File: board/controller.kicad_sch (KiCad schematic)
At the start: 26 parts, among them U3 W5500, Y2 25MHz

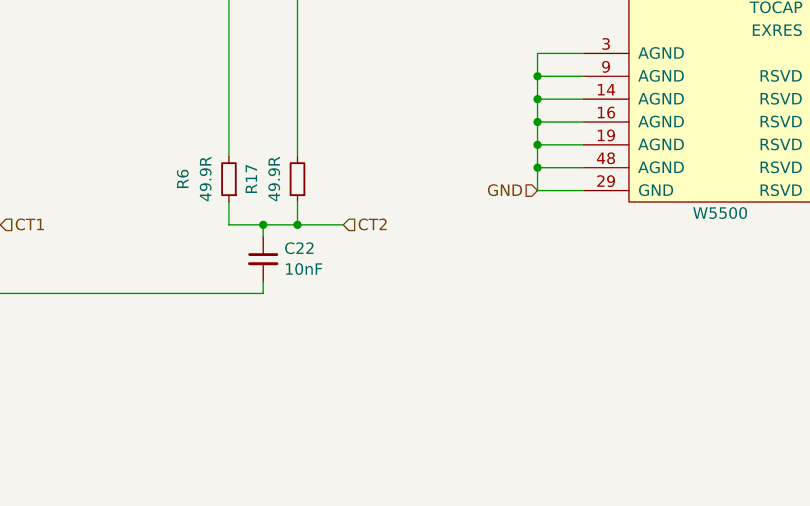
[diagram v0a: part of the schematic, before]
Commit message: updated to use v1.1 of b078 to work with shorted center tap magjacks
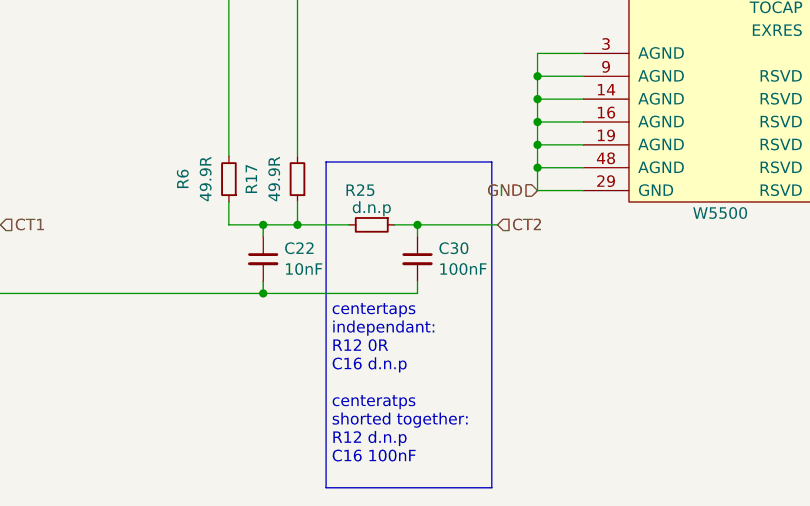
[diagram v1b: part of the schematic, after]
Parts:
- added C30: 100nF, Capacitor_SMD:C_0603_1608Metric, symbol Device:C_Small
- added R25: d.n.p, Resistor_SMD:R_0805_2012Metric, symbol Device:R_Small
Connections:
- net CT2: now also C30.1, R25.1; no longer C22.1, R17.1, R6.1
- net GND: now also C30.2
- new net: C22.1, R17.1, R25.2, R6.1
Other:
- note added: "centertaps independant: R12 0R C16 d.n.p centeratps shorted together: R12 d.n.p C16 100nF"
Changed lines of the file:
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@@
   (junction (at 176.53 92.71) (diameter 0) (color 0 0 0 0)
   )
+  (junction (at 96.52 87.63) (diameter 0) (color 0 0 0 0)
+  )
+  (junction (at 80.01 50.8) (diameter 0) (color 0 0 0 0)
+  )
+  (junction (at 105.41 49.53) (diameter 0) (color 0 0 0 0)
+  )
+  (junction (at 95.25 64.77) (diameter 0) (color 0 0 0 0)
+  )
+  (junction (at 179.07 116.84) (diameter 0) (color 0 0 0 0)
+  )
+  (junction (at 163.83 92.71) (diameter 0) (color 0 0 0 0)
+  )
+  (junction (at 176.53 82.55) (diameter 0) (color 0 0 0 0)
+  )
+  (junction (at 105.41 59.69) (diameter 0) (color 0 0 0 0)
+  )
+  (junction (at 72.39 64.77) (diameter 0) (color 0 0 0 0)
+  )
+  (junction (at 162.56 44.45) (diameter 0) (color 0 0 0 0)
+  )
+  (junction (at 162.56 113.03) (diameter 0) (color 0 0 0 0)
+  )
+  (junction (at 123.19 110.49) (diameter 0) (color 0 0 0 0)
+  )
+  (junction (at 163.83 82.55) (diameter 0) (color 0 0 0 0)
+  )
+  (junction (at 162.56 107.95) (diameter 0) (color 0 0 0 0)
+  )
+  (junction (at 87.63 50.8) (diameter 0) (color 0 0 0 0)
+  )
+  (junction (at 87.63 64.77) (diameter 0) (color 0 0 0 0)
+  )
+  (junction (at 62.23 92.71) (diameter 0) (color 0 0 0 0)
+  )
+  (junction (at 189.23 116.84) (diameter 0) (color 0 0 0 0)
+  )
+  (junction (at 105.41 54.61) (diameter 0) (color 0 0 0 0)
+  )
+  (junction (at 72.39 50.8) (diameter 0) (color 0 0 0 0)
+  )
+  (junction (at 88.9 90.17) (diameter 0) (color 0 0 0 0)
+  )
+  (junction (at 123.19 115.57) (diameter 0) (color 0 0 0 0)
+  )
+  (junction (at 162.56 116.84) (diameter 0) (color 0 0 0 0)
+  )
+  (junction (at 92.71 129.54) (diameter 0) (color 0 0 0 0)
+  )
+  (junction (at 109.855 121.92) (diameter 0) (color 0 0 0 0)
+  )
   (junction (at 96.52 121.92) (diameter 0) (color 0 0 0 0)
-  )
-  (junction (at 96.52 87.63) (diameter 0) (color 0 0 0 0)
-  )
-  (junction (at 80.01 50.8) (diameter 0) (color 0 0 0 0)
-  )
-  (junction (at 105.41 49.53) (diameter 0) (color 0 0 0 0)
-  )
-  (junction (at 95.25 64.77) (diameter 0) (color 0 0 0 0)
-  )
-  (junction (at 179.07 116.84) (diameter 0) (color 0 0 0 0)
-  )
-  (junction (at 163.83 92.71) (diameter 0) (color 0 0 0 0)
-  )
-  (junction (at 176.53 82.55) (diameter 0) (color 0 0 0 0)
-  )
-  (junction (at 105.41 59.69) (diameter 0) (color 0 0 0 0)
-  )
-  (junction (at 72.39 64.77) (diameter 0) (color 0 0 0 0)
-  )
-  (junction (at 162.56 44.45) (diameter 0) (color 0 0 0 0)
-  )
-  (junction (at 162.56 113.03) (diameter 0) (color 0 0 0 0)
-  )
-  (junction (at 123.19 110.49) (diameter 0) (color 0 0 0 0)
-  )
-  (junction (at 163.83 82.55) (diameter 0) (color 0 0 0 0)
-  )
-  (junction (at 162.56 107.95) (diameter 0) (color 0 0 0 0)
-  )
-  (junction (at 87.63 50.8) (diameter 0) (color 0 0 0 0)
-  )
-  (junction (at 87.63 64.77) (diameter 0) (color 0 0 0 0)
-  )
-  (junction (at 62.23 92.71) (diameter 0) (color 0 0 0 0)
-  )
-  (junction (at 189.23 116.84) (diameter 0) (color 0 0 0 0)
-  )
-  (junction (at 105.41 54.61) (diameter 0) (color 0 0 0 0)
-  )
-  (junction (at 72.39 50.8) (diameter 0) (color 0 0 0 0)
-  )
-  (junction (at 88.9 90.17) (diameter 0) (color 0 0 0 0)
-  )
-  (junction (at 123.19 115.57) (diameter 0) (color 0 0 0 0)
-  )
-  (junction (at 162.56 116.84) (diameter 0) (color 0 0 0 0)
   )
   (junction (at 69.85 95.25) (diameter 0) (color 0 0 0 0)
@@
     (stroke (width 0) (type default) (color 0 0 0 0))
   )
-  (wire (pts (xy 96.52 121.92) (xy 101.6 121.92))
-    (stroke (width 0) (type default) (color 0 0 0 0))
-  )
   (wire (pts (xy 88.9 90.17) (xy 102.87 90.17))
     (stroke (width 0) (type default) (color 0 0 0 0))
@@
     (stroke (width 0) (type default) (color 0 0 0 0))
   )
+  (polyline (pts (xy 99.695 151.13) (xy 118.11 151.13))
+    (stroke (width 0) (type default) (color 0 0 0 0))
+  )
   (wire (pts (xy 128.27 49.53) (xy 105.41 49.53))
     (stroke (width 0) (type default) (color 0 0 0 0))
@@
     (stroke (width 0) (type default) (color 0 0 0 0))
   )
+  (polyline (pts (xy 118.11 114.935) (xy 99.695 114.935))
+    (stroke (width 0) (type default) (color 0 0 0 0))
+  )
   (wire (pts (xy 105.41 54.61) (xy 105.41 52.07))
     (stroke (width 0) (type default) (color 0 0 0 0))
@@
     (stroke (width 0) (type default) (color 0 0 0 0))
   )
+  (wire (pts (xy 118.745 121.92) (xy 109.855 121.92))
+    (stroke (width 0) (type default) (color 0 0 0 0))
+  )
   (wire (pts (xy 123.19 110.49) (xy 123.19 113.03))
     (stroke (width 0) (type default) (color 0 0 0 0))
@@
     (stroke (width 0) (type default) (color 0 0 0 0))
   )
+  (wire (pts (xy 109.855 121.92) (xy 109.855 123.19))
+    (stroke (width 0) (type default) (color 0 0 0 0))
+  )
   (wire (pts (xy 83.82 90.17) (xy 88.9 90.17))
     (stroke (width 0) (type default) (color 0 0 0 0))
@@
     (stroke (width 0) (type default) (color 0 0 0 0))
   )
+  (wire (pts (xy 107.315 121.92) (xy 109.855 121.92))
+    (stroke (width 0) (type default) (color 0 0 0 0))
+  )
+  (polyline (pts (xy 99.695 114.935) (xy 99.695 151.13))
+    (stroke (width 0) (type default) (color 0 0 0 0))
+  )
   (wire (pts (xy 95.25 50.8) (xy 105.41 50.8))
     (stroke (width 0) (type default) (color 0 0 0 0))
@@
     (stroke (width 0) (type default) (color 0 0 0 0))
   )
+  (wire (pts (xy 92.71 129.54) (xy 109.855 129.54))
+    (stroke (width 0) (type default) (color 0 0 0 0))
+  )
   (wire (pts (xy 162.56 38.1) (xy 162.56 44.45))
     (stroke (width 0) (type default) (color 0 0 0 0))
@@
     (stroke (width 0) (type default) (color 0 0 0 0))
   )
+  (wire (pts (xy 96.52 121.92) (xy 102.235 121.92))
+    (stroke (width 0) (type default) (color 0 0 0 0))
+  )
   (wire (pts (xy 96.52 121.92) (xy 96.52 119.38))
     (stroke (width 0) (type default) (color 0 0 0 0))
   )
+  (wire (pts (xy 109.855 129.54) (xy 109.855 128.27))
+    (stroke (width 0) (type default) (color 0 0 0 0))
+  )
   (wire (pts (xy 69.85 95.25) (xy 114.3 95.25))
     (stroke (width 0) (type default) (color 0 0 0 0))
@@
   (wire (pts (xy 128.27 52.07) (xy 105.41 52.07))
     (stroke (width 0) (type default) (color 0 0 0 0))
+  )
+  (polyline (pts (xy 118.11 114.935) (xy 118.11 151.13))
+    (stroke (width 0) (type default) (color 0 0 0 0))
+  )
+  (text "centertaps \nindependant:\nR12 0R\nC16 d.n.p\n\ncenteratps\nshorted together:\nR12 d.n.p\nC16 100nF"
+    (at 100.33 148.59 0)
+    (effects (font (size 1.27 1.27)) (justify left bottom))
   )
   (label "XCAP" (at 160.02 97.79 0)
@@
     (effects (font (size 1.27 1.27)) (justify right))
   )
-  (hierarchical_label "CT2" (shape input) (at 101.6 121.92 0)
-    (effects (font (size 1.27 1.27)) (justify left))
-  )
   (hierarchical_label "GND" (shape input) (at 123.19 118.11 180)
     (effects (font (size 1.27 1.27)) (justify right))
@@
   )
   (hierarchical_label "INT" (shape input) (at 190.5 64.77 0)
+    (effects (font (size 1.27 1.27)) (justify left))
+  )
+  (hierarchical_label "CT2" (shape input) (at 118.745 121.92 0)
     (effects (font (size 1.27 1.27)) (justify left))
   )
@@
     )
     (property "Datasheet" "~" (id 3) (at 116.84 95.25 0)
+      (effects (font (size 1.27 1.27)) hide)
+    )
+    (pin "1")
+    (pin "2")
+  )
+  (symbol (lib_id "Device:R_Small") (at 104.775 121.92 270) (unit 1)
+    (in_bom yes) (on_board yes)
+    (property "Reference" "R25" (id 0) (at 103.505 118.11 90))
+    (property "Value" "d.n.p" (id 1) (at 104.775 120.015 90))
+    (property "Footprint" "Resistor_SMD:R_0805_2012Metric" (id 2) (at 104.775 121.92 0)
+      (effects (font (size 1.27 1.27)) hide)
+    )
+    (property "Datasheet" "~" (id 3) (at 104.775 121.92 0)
       (effects (font (size 1.27 1.27)) hide)
     )
@@
     (pin "9")
   )
+  (symbol (lib_id "Device:C_Small") (at 109.855 125.73 0) (unit 1)
+    (in_bom yes) (on_board yes)
+    (property "Reference" "C30" (id 0) (at 112.1918 124.5616 0)
+      (effects (font (size 1.27 1.27)) (justify left))
+    )
+    (property "Value" "100nF" (id 1) (at 112.1918 126.873 0)
+      (effects (font (size 1.27 1.27)) (justify left))
+    )
+    (property "Footprint" "Capacitor_SMD:C_0603_1608Metric" (id 2) (at 109.855 125.73 0)
+      (effects (font (size 1.27 1.27)) hide)
+    )
+    (property "Datasheet" "~" (id 3) (at 109.855 125.73 0)
+      (effects (font (size 1.27 1.27)) hide)
+    )
+    (property "Voltage" "6.3V" (id 4) (at 109.855 125.73 0)
+      (effects (font (size 1.27 1.27)) hide)
+    )
+    (pin "1")
+    (pin "2")
+  )
   (symbol (lib_id "Device:R_Small") (at 110.49 87.63 90) (unit 1)

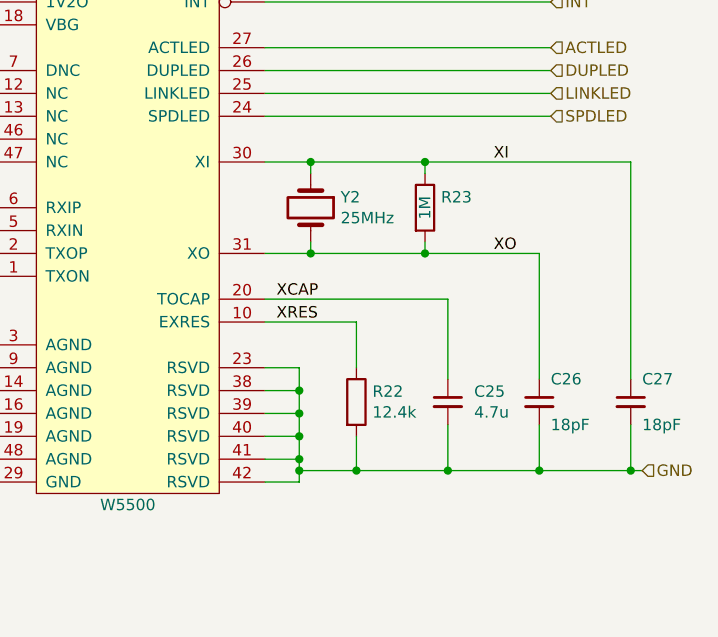
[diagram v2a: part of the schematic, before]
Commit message: moved all components to top layer
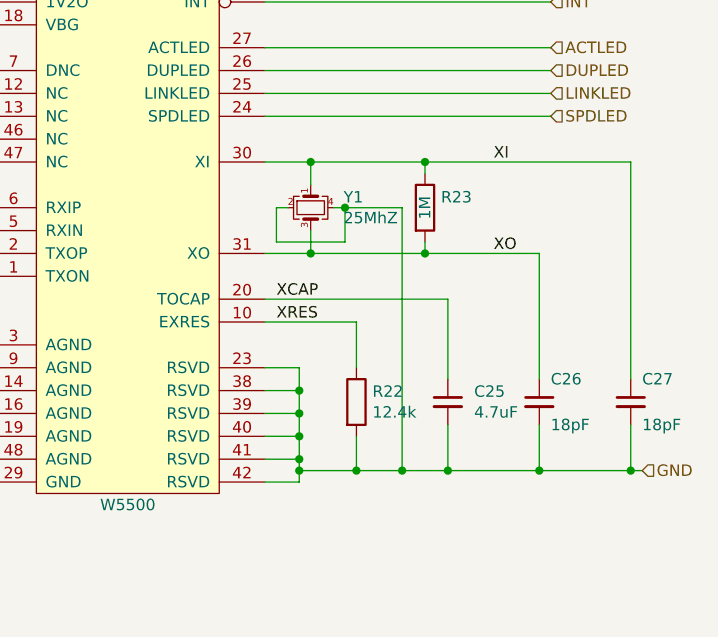
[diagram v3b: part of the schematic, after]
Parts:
- removed Y2: 25MHz, Crystal:Crystal_SMD_5032-2Pin_5.0x3.2mm, symbol Device:Crystal
- added Y1: 25MhZ, Crystal:Crystal_SMD_Abracon_ABM8G-4Pin_3.2x2.5mm, symbol Device:Crystal_GND24_Small
- C16, C17, C19, C21, C22, C23, C26, C27, C30: footprint Capacitor_SMD:C_0603_1608Metric -> Capacitor_SMD:C_0402_1005Metric
- C24: footprint Capacitor_SMD:C_0603_1608Metric -> Capacitor_SMD:C_0402_1005Metric; DigiKey Part Number 1276-1921-1-ND -> (none)
- C25: value 4.7u -> 4.7uF; footprint Capacitor_SMD:C_0603_1608Metric -> Capacitor_SMD:C_0402_1005Metric; DigiKey Part Number 1276-1907-1-ND -> (none)
- R23: footprint Resistor_SMD:R_0603_1608Metric -> Resistor_SMD:R_0402_1005Metric
- R3: footprint Resistor_SMD:R_0805_2012Metric -> Resistor_SMD:R_0603_1608Metric
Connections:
- net GND: now also Y1.2, Y1.4
- net XI: now also Y1.1
- net XO: now also Y1.3
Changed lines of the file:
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@@
   (junction (at 105.41 49.53) (diameter 0) (color 0 0 0 0)
   )
+  (junction (at 167.64 87.63) (diameter 0) (color 0 0 0 0)
+  )
   (junction (at 95.25 64.77) (diameter 0) (color 0 0 0 0)
   )
@@
   )
   (junction (at 162.56 110.49) (diameter 0) (color 0 0 0 0)
+  )
+  (junction (at 173.99 116.84) (diameter 0) (color 0 0 0 0)
   )
   (junction (at 95.25 50.8) (diameter 0) (color 0 0 0 0)
@@
     (stroke (width 0) (type default))
   )
-  (wire (pts (xy 163.83 92.71) (xy 163.83 91.44))
+  (wire (pts (xy 163.83 90.17) (xy 163.83 92.71))
     (stroke (width 0) (type default))
   )
@@
     (stroke (width 0) (type default))
   )
-  (wire (pts (xy 168.91 116.84) (xy 179.07 116.84))
+  (wire (pts (xy 168.91 116.84) (xy 173.99 116.84))
     (stroke (width 0) (type default))
   )
@@
     (stroke (width 0) (type default))
   )
+  (wire (pts (xy 173.99 116.84) (xy 179.07 116.84))
+    (stroke (width 0) (type default))
+  )
   (wire (pts (xy 87.63 64.77) (xy 80.01 64.77))
     (stroke (width 0) (type default))
@@
     (stroke (width 0) (type default))
   )
+  (wire (pts (xy 167.64 87.63) (xy 166.37 87.63))
+    (stroke (width 0) (type default))
+  )
   (wire (pts (xy 72.39 64.77) (xy 64.77 64.77))
     (stroke (width 0) (type default))
@@
     (stroke (width 0) (type default))
   )
+  (wire (pts (xy 173.99 116.84) (xy 173.99 87.63))
+    (stroke (width 0) (type default))
+  )
   (polyline (pts (xy 99.695 114.935) (xy 99.695 151.13))
     (stroke (width 0) (type default))
@@
     (stroke (width 0) (type default))
   )
+  (wire (pts (xy 173.99 87.63) (xy 167.64 87.63))
+    (stroke (width 0) (type default))
+  )
   (wire (pts (xy 162.56 116.84) (xy 162.56 115.57))
     (stroke (width 0) (type default))
@@
     (stroke (width 0) (type default))
   )
+  (wire (pts (xy 167.64 87.63) (xy 167.64 91.44))
+    (stroke (width 0) (type default))
+  )
   (wire (pts (xy 55.88 129.54) (xy 92.71 129.54))
     (stroke (width 0) (type default))
@@
     (stroke (width 0) (type default))
   )
+  (wire (pts (xy 167.64 91.44) (xy 160.02 91.44))
+    (stroke (width 0) (type default))
+  )
   (wire (pts (xy 58.42 92.71) (xy 62.23 92.71))
     (stroke (width 0) (type default))
@@
     (stroke (width 0) (type default))
   )
+  (wire (pts (xy 160.02 91.44) (xy 160.02 87.63))
+    (stroke (width 0) (type default))
+  )
   (wire (pts (xy 96.52 121.92) (xy 96.52 119.38))
     (stroke (width 0) (type default))
@@
     (stroke (width 0) (type default))
   )
+  (wire (pts (xy 160.02 87.63) (xy 161.29 87.63))
+    (stroke (width 0) (type default))
+  )
   (wire (pts (xy 87.63 60.96) (xy 87.63 64.77))
     (stroke (width 0) (type default))
@@
     (stroke (width 0) (type default))
   )
-  (wire (pts (xy 163.83 82.55) (xy 163.83 83.82))
+  (wire (pts (xy 163.83 82.55) (xy 163.83 85.09))
     (stroke (width 0) (type default))
   )
@@
       (effects (font (size 1.27 1.27)) (justify left))
     )
-    (property "Footprint" "Capacitor_SMD:C_0603_1608Metric" (at 95.25 58.42 0)
+    (property "Footprint" "Capacitor_SMD:C_0402_1005Metric" (at 95.25 58.42 0)
       (effects (font (size 1.27 1.27)) hide)
     )
@@
       (effects (font (size 1.27 1.27)) (justify left))
     )
-    (property "Value" "4.7u" (at 181.991 110.363 0)
-      (effects (font (size 1.27 1.27)) (justify left))
-    )
-    (property "Footprint" "Capacitor_SMD:C_0603_1608Metric" (at 179.07 109.22 0)
+    (property "Value" "4.7uF" (at 181.991 110.363 0)
+      (effects (font (size 1.27 1.27)) (justify left))
+    )
+    (property "Footprint" "Capacitor_SMD:C_0402_1005Metric" (at 179.07 109.22 0)
       (effects (font (size 1.27 1.27)) hide)
     )
@@
       (effects (font (size 1.27 1.27)) hide)
     )
-    (property "DigiKey Part Number" "1276-1907-1-ND" (at 179.07 109.22 0)
-      (effects (font (size 1.27 1.27)) hide)
-    )
     (pin "1")
     (pin "2")
@@
       (effects (font (size 1.27 1.27)) (justify left))
     )
-    (property "Footprint" "Capacitor_SMD:C_0603_1608Metric" (at 80.01 58.42 0)
+    (property "Footprint" "Capacitor_SMD:C_0402_1005Metric" (at 80.01 58.42 0)
       (effects (font (size 1.27 1.27)) hide)
     )
@@
       (effects (font (size 1.27 1.27)))
     )
-    (property "Footprint" "Resistor_SMD:R_0603_1608Metric" (at 174.752 87.63 90)
+    (property "Footprint" "Resistor_SMD:R_0402_1005Metric" (at 174.752 87.63 90)
       (effects (font (size 1.27 1.27)) hide)
     )
@@
       (effects (font (size 1.27 1.27)) (justify left))
     )
-    (property "Footprint" "Capacitor_SMD:C_0603_1608Metric" (at 109.855 125.73 0)
+    (property "Footprint" "Capacitor_SMD:C_0402_1005Metric" (at 109.855 125.73 0)
       (effects (font (size 1.27 1.27)) hide)
     )
@@
       (effects (font (size 1.27 1.27)) (justify left))
     )
-    (property "Footprint" "Capacitor_SMD:C_0603_1608Metric" (at 64.77 58.42 0)
+    (property "Footprint" "Capacitor_SMD:C_0402_1005Metric" (at 64.77 58.42 0)
       (effects (font (size 1.27 1.27)) hide)
     )
@@
       (effects (font (size 1.27 1.27)) (justify left))
     )
-    (property "Footprint" "Capacitor_SMD:C_0603_1608Metric" (at 92.71 125.73 0)
+    (property "Footprint" "Capacitor_SMD:C_0402_1005Metric" (at 92.71 125.73 0)
       (effects (font (size 1.27 1.27)) hide)
     )
@@
       (effects (font (size 1.27 1.27)))
     )
-    (property "Footprint" "Resistor_SMD:R_0805_2012Metric" (at 55.88 118.11 0)
+    (property "Footprint" "Resistor_SMD:R_0603_1608Metric" (at 55.88 118.11 0)
       (effects (font (size 1.27 1.27)) hide)
     )
@@
       (effects (font (size 1.27 1.27)) (justify left))
     )
-    (property "Footprint" "Capacitor_SMD:C_0603_1608Metric" (at 87.63 58.42 0)
+    (property "Footprint" "Capacitor_SMD:C_0402_1005Metric" (at 87.63 58.42 0)
       (effects (font (size 1.27 1.27)) hide)
     )
@@
     )
   )
+  (symbol (lib_id "Device:Crystal_GND24_Small") (at 163.83 87.63 270) (unit 1)
+    (in_bom yes) (on_board yes) (dnp no)
+    (property "Reference" "Y1" (at 167.4876 86.4616 90)
+      (effects (font (size 1.27 1.27)) (justify left))
+    )
+    (property "Value" "25MhZ" (at 167.4876 88.773 90)
+      (effects (font (size 1.27 1.27)) (justify left))
+    )
+    (property "Footprint" "Crystal:Crystal_SMD_Abracon_ABM8G-4Pin_3.2x2.5mm" (at 163.83 87.63 0)
+      (effects (font (size 1.27 1.27)) hide)
+    )
+    (property "Datasheet" "~" (at 163.83 87.63 0)
+      (effects (font (size 1.27 1.27)) hide)
+    )
+    (pin "1")
+    (pin "2")
+    (pin "3")
+    (pin "4")
+    (instances
+      (project "board"
+        (path "/57732dd3-1162-4c3f-88bd-31bf473d124d/767ce4c6-0e55-4543-92f0-34cb8237a544"
+          (reference "Y1") (unit 1)
+        )
+        (path "/57732dd3-1162-4c3f-88bd-31bf473d124d/861c2f1b-c8f0-4d7b-be1f-ed76d698b8b8"
+          (reference "Y2") (unit 1)
+        )
+      )
+    )
+  )
   (symbol (lib_id "Device:C_Small") (at 189.23 109.22 0) (unit 1)
     (in_bom yes) (on_board yes) (dnp no)
@@
       (effects (font (size 1.27 1.27)) (justify left))
     )
-    (property "Footprint" "Capacitor_SMD:C_0603_1608Metric" (at 189.23 109.22 0)
+    (property "Footprint" "Capacitor_SMD:C_0402_1005Metric" (at 189.23 109.22 0)
       (effects (font (size 1.27 1.27)) hide)
     )
@@
       (effects (font (size 1.27 1.27)) (justify left))
     )
-    (property "Footprint" "Capacitor_SMD:C_0603_1608Metric" (at 199.39 109.22 0)
+    (property "Footprint" "Capacitor_SMD:C_0402_1005Metric" (at 199.39 109.22 0)
       (effects (font (size 1.27 1.27)) hide)
     )
@@
       (effects (font (size 1.27 1.27)) (justify left))
     )
-    (property "Footprint" "Capacitor_SMD:C_0603_1608Metric" (at 113.03 64.77 0)
+    (property "Footprint" "Capacitor_SMD:C_0402_1005Metric" (at 113.03 64.77 0)
       (effects (font (size 1.27 1.27)) hide)
     )
@@
       (effects (font (size 1.27 1.27)) hide)
     )
-    (property "DigiKey Part Number" "1276-1921-1-ND" (at 113.03 64.77 0)
-      (effects (font (size 1.27 1.27)) hide)
-    )
     (pin "1")
     (pin "2")
@@
       (effects (font (size 1.27 1.27)) (justify left))
     )
-    (property "Footprint" "Capacitor_SMD:C_0603_1608Metric" (at 72.39 58.42 0)
+    (property "Footprint" "Capacitor_SMD:C_0402_1005Metric" (at 72.39 58.42 0)
       (effects (font (size 1.27 1.27)) hide)
     )
@@
         )
       )
-    )
-  )
-  (symbol (lib_id "Device:Crystal") (at 163.83 87.63 270) (unit 1)
-    (in_bom yes) (on_board yes) (dnp no)
-    (property "Reference" "Y2" (at 167.1574 86.4616 90)
-      (effects (font (size 1.27 1.27)) (justify left))
-    )
-    (property "Value" "25MHz" (at 167.1574 88.773 90)
-      (effects (font (size 1.27 1.27)) (justify left))
-    )
-    (property "Footprint" "Crystal:Crystal_SMD_5032-2Pin_5.0x3.2mm" (at 163.83 87.63 0)
-      (effects (font (size 1.27 1.27)) hide)
-    )
-    (property "Datasheet" "~" (at 163.83 87.63 0)
-      (effects (font (size 1.27 1.27)) hide)
-    )
-    (property "DigiKey Part Number" "CTX1175TR-ND" (at 163.83 87.63 90)
-      (effects (font (size 1.27 1.27)) hide)
-    )
-    (property "MPN" "445I23D25M00000" (at 163.83 87.63 90)
-      (effects (font (size 1.27 1.27)) hide)
-    )
-    (pin "1")
-    (pin "2")
-    (instances
-      (project "board"
-        (path "/57732dd3-1162-4c3f-88bd-31bf473d124d/861c2f1b-c8f0-4d7b-be1f-ed76d698b8b8"
-          (reference "Y2") (unit 1)
-        )
-      )
